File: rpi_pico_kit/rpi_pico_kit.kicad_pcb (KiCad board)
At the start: 2 copper layers, 99.1 x 99.1 mm, 200 parts, among them J1 DC Jack 5.5x2.1mm, J10 OLED Display SSD1306, J11 Conn_01x04_Male, J12 Conn_01x04_Male, J13 AudioJack-CUI-SJ-3523-SMT, J14 AudioJack-CUI-SJ-3523-SMT, J2 USB_B, J3 Conn_01x03_Male, J4 DB15_Female, J5 HDMI_A, J6 Conn_01x08_Male, J7 Conn_01x08_Male, J8 Conn_01x08_Male, J9 Micro_SD_Card_Det, Q1 DMN63D8L-7, Q2 DMN63D8L-7, Q3 DMN63D8L-7, Q4 DMN63D8L-7, Q5 DMN63D8L-7, Q6 DMN63D8L-7, Q7 DMN63D8L-7, SW1 SW_Push, SW10 SW_Push, SW2 RotaryEncoder_Switch, SW3 SW_Push, SW4 SW_Push, SW5 SW_Push, SW6 SW_Push, SW7 SW_Push, SW8 SW_Push, SW9 SW_Push, U1 RPi Pico, U10 74LVC2G34GV, U11 PCM5101A, U2 NCP1117-3.3_SOT223, U3 RP2040, U4 W25Q16JVSSIQ, U5 74HC14, U6 74HC14, U7 MCP23S08-xSO, U8 AT24CS32, U9 NCP115-3.3_SOT23-5, Y1 12MHz

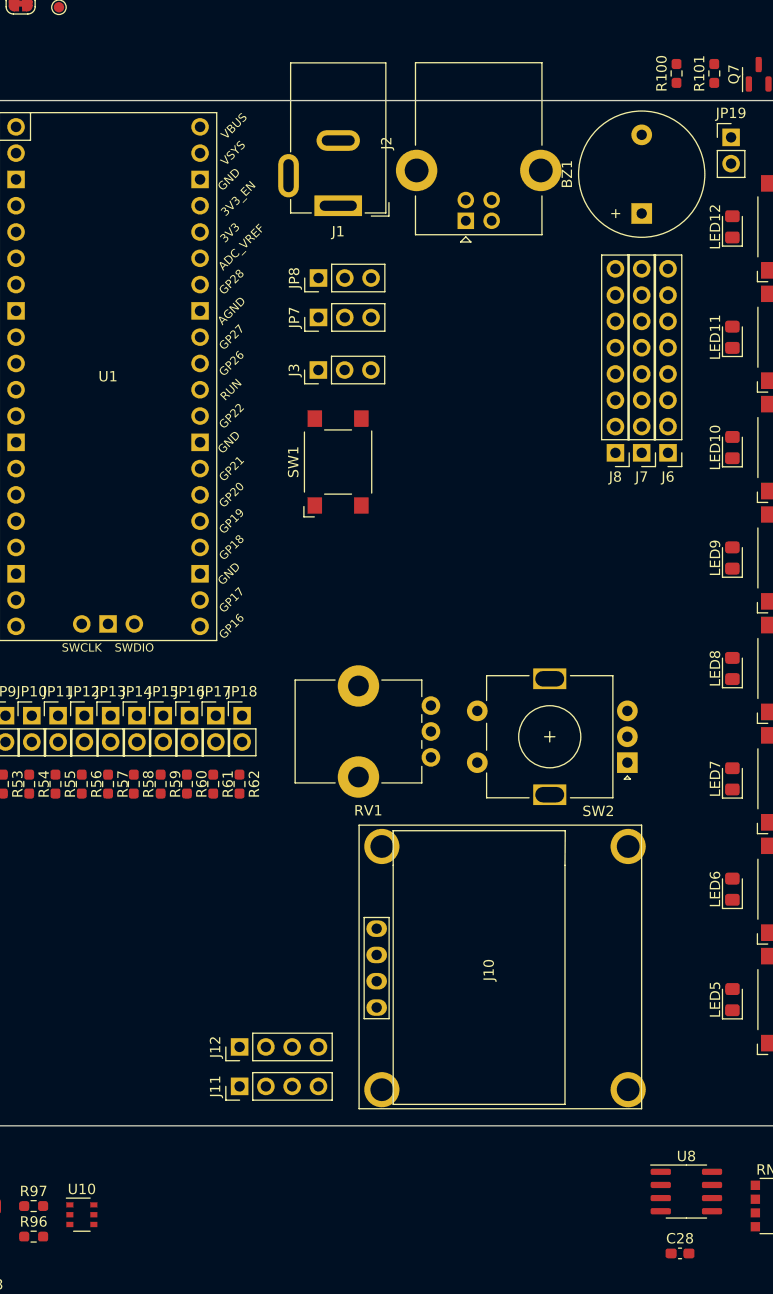
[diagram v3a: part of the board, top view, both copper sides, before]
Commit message: changed footprint U10
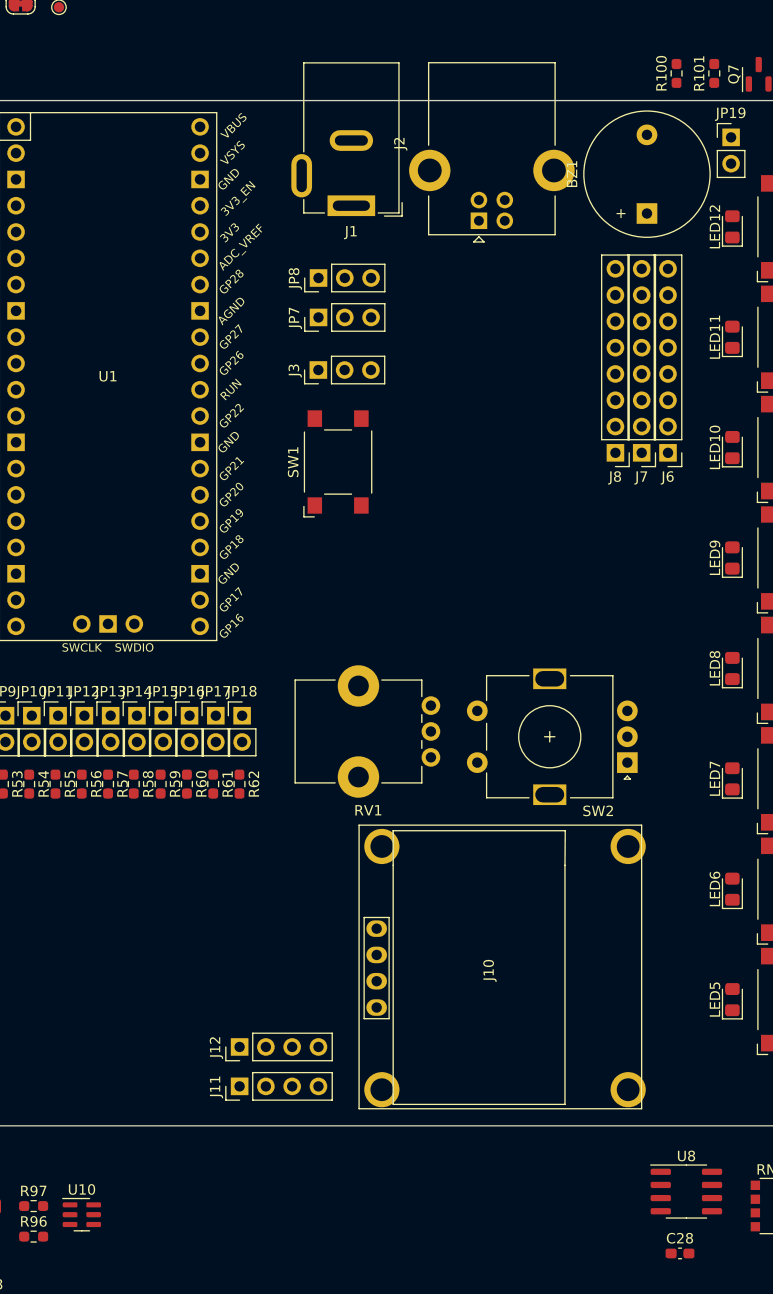
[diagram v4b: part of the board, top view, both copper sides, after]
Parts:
- U10: footprint Package_SO:TSOP-6_1.65x3.05mm_P0.95mm -> Package_SO:SC-74-6_1.5x2.9mm_P0.95mm
- moved J2 1.27 mm to (103.1, 49.7)
- moved J1 1.27 mm to (90.8, 48.3)
- moved BZ1 0.51 mm to (119.4, 49.0)
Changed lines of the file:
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@@
     )
   )
-  (footprint "Package_SO:TSOP-6_1.65x3.05mm_P0.95mm" (layer "F.Cu")
+  (footprint "Package_SO:SC-74-6_1.5x2.9mm_P0.95mm" (layer "F.Cu")
     (at 64.78 145.745)
-    (descr "TSOP-6 package (comparable to TSOT-23), https://www.vishay.com/docs/71200/71200.pdf")
-    (tags "Jedec MO-193C TSOP-6L")
+    (descr "SC-74, 6 Pin (https://www.nxp.com/docs/en/package-information/SOT457.pdf), generated with kicad-footprint-generator ipc_gullwing_generator.py")
+    (tags "SC-74 SO")
     (property "Manufacturer Part Number" "74LVC2G34GV,125")
     (property "Sheetfile" "audio.kicad_sch")
@@
     (property "Supplier Part URL" "https://www.digikey.cz/en/products/detail/nexperia-usa-inc/74LVC2G34GV-125/1231596")
     (attr smd)
-    (fp_text reference "U10" (at 0 -2.45) (layer "F.SilkS")
+    (fp_text reference "U10" (at 0 -2.4) (layer "F.SilkS")
         (effects (font (size 1 1) (thickness 0.15)))
     )
-    (fp_text value "74LVC2G34GV" (at 0 2.5) (layer "F.Fab")
+    (fp_text value "74LVC2G34GV" (at 0 2.4) (layer "F.Fab")
         (effects (font (size 1 1) (thickness 0.15)))
     )
-    (fp_text user "${REFERENCE}" (at 0 0 90) (layer "F.Fab")
-        (effects (font (size 0.5 0.5) (thickness 0.075)))
+    (fp_text user "${REFERENCE}" (at 0 0) (layer "F.Fab")
+        (effects (font (size 0.38 0.38) (thickness 0.06)))
     )
-    (fp_line (start -0.8 1.6) (end 0.8 1.6)
+    (fp_line (start 0 -1.56) (end -1.85 -1.56)
+      (stroke (width 0.12) (type solid)) (layer "F.SilkS"))
+    (fp_line (start 0 -1.56) (end 0.75 -1.56)
+      (stroke (width 0.12) (type solid)) (layer "F.SilkS"))
+    (fp_line (start 0 1.56) (end -0.75 1.56)
       (stroke (width 0.12) (type solid)) (layer "F.SilkS"))
-    (fp_line (start 0.8 -1.6) (end -1.5 -1.6)
+    (fp_line (start 0 1.56) (end 0.75 1.56)
       (stroke (width 0.12) (type solid)) (layer "F.SilkS"))
-    (fp_line (start -1.76 -1.78) (end -1.76 1.77)
+    (fp_line (start -2.1 -1.7) (end -2.1 1.7)
       (stroke (width 0.05) (type solid)) (layer "F.CrtYd"))
-    (fp_line (start -1.76 -1.78) (end 1.76 -1.78)
+    (fp_line (start -2.1 1.7) (end 2.1 1.7)
       (stroke (width 0.05) (type solid)) (layer "F.CrtYd"))
-    (fp_line (start 1.76 1.77) (end -1.76 1.77)
+    (fp_line (start 2.1 -1.7) (end -2.1 -1.7)
       (stroke (width 0.05) (type solid)) (layer "F.CrtYd"))
-    (fp_line (start 1.76 1.77) (end 1.76 -1.78)
+    (fp_line (start 2.1 1.7) (end 2.1 -1.7)
       (stroke (width 0.05) (type solid)) (layer "F.CrtYd"))
-    (fp_line (start -0.825 -1.1) (end -0.825 1.525)
+    (fp_line (start -0.75 -1.075) (end -0.375 -1.45)
       (stroke (width 0.1) (type solid)) (layer "F.Fab"))
-    (fp_line (start -0.825 -1.1) (end -0.425 -1.525)
+    (fp_line (start -0.75 1.45) (end -0.75 -1.075)
       (stroke (width 0.1) (type solid)) (layer "F.Fab"))
-    (fp_line (start 0.825 -1.525) (end -0.425 -1.525)
+    (fp_line (start -0.375 -1.45) (end 0.75 -1.45)
       (stroke (width 0.1) (type solid)) (layer "F.Fab"))
-    (fp_line (start 0.825 -1.525) (end 0.825 1.525)
+    (fp_line (start 0.75 -1.45) (end 0.75 1.45)
       (stroke (width 0.1) (type solid)) (layer "F.Fab"))
-    (fp_line (start 0.825 1.525) (end -0.825 1.525)
+    (fp_line (start 0.75 1.45) (end -0.75 1.45)
       (stroke (width 0.1) (type solid)) (layer "F.Fab"))
-    (pad "1" smd rect (at -1.16 -0.95) (size 0.7 0.51) (layers "F.Cu" "F.Paste" "F.Mask")
+    (pad "1" smd roundrect (at -1.1375 -0.95) (size 1.425 0.5) (layers "F.Cu" "F.Paste" "F.Mask") (roundrect_rratio 0.25)
       (net 136 "/I2S_LRCK") (pinfunction "A1") (pintype "input"))
-    (pad "2" smd rect (at -1.16 0) (size 0.7 0.51) (layers "F.Cu" "F.Paste" "F.Mask")
+    (pad "2" smd roundrect (at -1.1375 0) (size 1.425 0.5) (layers "F.Cu" "F.Paste" "F.Mask") (roundrect_rratio 0.25)
       (net 3 "GND") (pinfunction "GND") (pintype "power_in"))
-    (pad "3" smd rect (at -1.16 0.95) (size 0.7 0.51) (layers "F.Cu" "F.Paste" "F.Mask")
+    (pad "3" smd roundrect (at -1.1375 0.95) (size 1.425 0.5) (layers "F.Cu" "F.Paste" "F.Mask") (roundrect_rratio 0.25)
       (net 137 "/I2S_BCK") (pinfunction "A2") (pintype "input"))
-    (pad "4" smd rect (at 1.16 0.95) (size 0.7 0.51) (layers "F.Cu" "F.Paste" "F.Mask")
+    (pad "4" smd roundrect (at 1.1375 0.95) (size 1.425 0.5) (layers "F.Cu" "F.Paste" "F.Mask") (roundrect_rratio 0.25)
       (net 151 "Net-(U10-Y2)") (pinfunction "Y2") (pintype "output"))
-    (pad "5" smd rect (at 1.16 0) (size 0.7 0.51) (layers "F.Cu" "F.Paste" "F.Mask")
+    (pad "5" smd roundrect (at 1.1375 0) (size 1.425 0.5) (layers "F.Cu" "F.Paste" "F.Mask") (roundrect_rratio 0.25)
       (net 12 "+3.3VA") (pinfunction "VCC") (pintype "power_in"))
-    (pad "6" smd rect (at 1.16 -0.95) (size 0.7 0.51) (layers "F.Cu" "F.Paste" "F.Mask")
+    (pad "6" smd roundrect (at 1.1375 -0.95) (size 1.425 0.5) (layers "F.Cu" "F.Paste" "F.Mask") (roundrect_rratio 0.25)
       (net 150 "Net-(U10-Y1)") (pinfunction "Y1") (pintype "output"))
     (model "${KICAD6_3DMODEL_DIR}/Package_SO.3dshapes/TSOP-6_1.65x3.05mm_P0.95mm.wrl"
@@
   )
   (footprint "Connector_BarrelJack:BarrelJack_GCT_DCJ200-10-A_Horizontal" (layer "F.Cu")
-    (at 89.55 48.26 180)
+    (at 90.82 48.26 180)
     (descr "Barrel jack connector (5.5 mm outer diameter, 2.05 inner diameter ), https://gct.co/files/drawings/dcj200-10.pdf")
     (tags "connector barrel jack")
@@
   )
   (footprint "Buzzer_Beeper:Buzzer_12x9.5RM7.6" (layer "F.Cu")
-    (at 118.872 49.012 90)
+    (at 119.38 49.012 90)
     (descr "Generic Buzzer, D12mm height 9.5mm with RM7.6mm")
     (tags "buzzer")
@@
   )
   (footprint "Connector_USB:USB_B_Lumberg_2411_02_Horizontal" (layer "F.Cu")
-    (at 101.874 49.7135 90)
+    (at 103.144 49.7135 90)
     (descr "USB 2.0 receptacle type B, horizontal version, through-hole, https://downloads.lumberg.com/datenblaetter/en/2411_02.pdf")
     (tags "USB B receptacle horizontal through-hole")

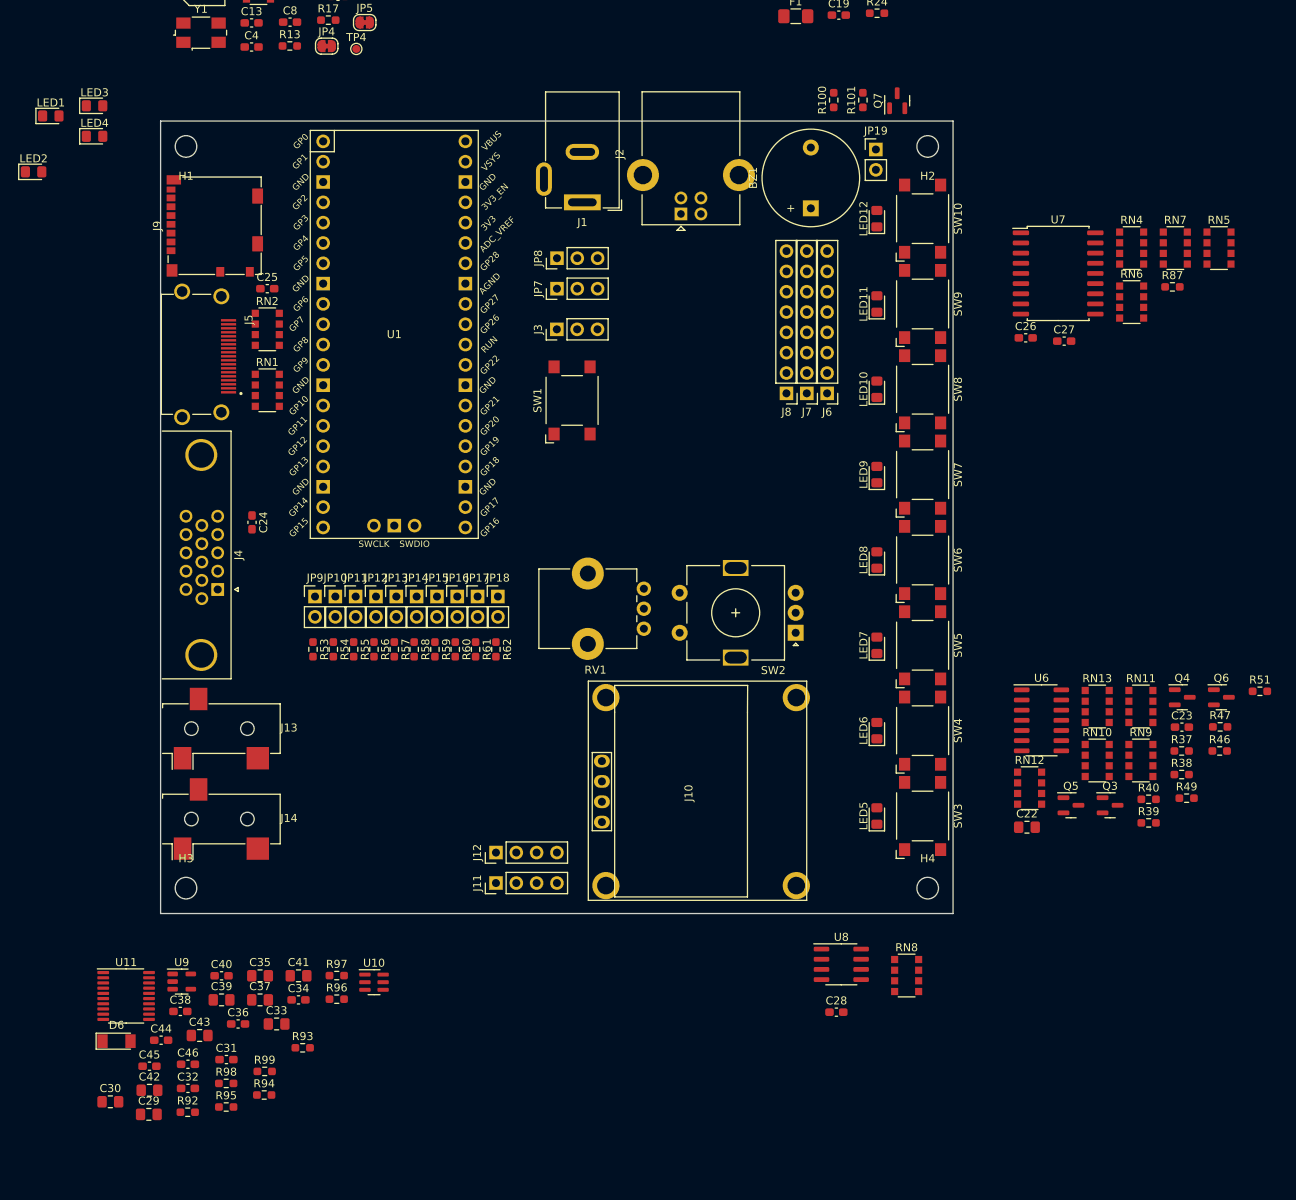
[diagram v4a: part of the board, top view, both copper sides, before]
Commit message: SPI conflict solved
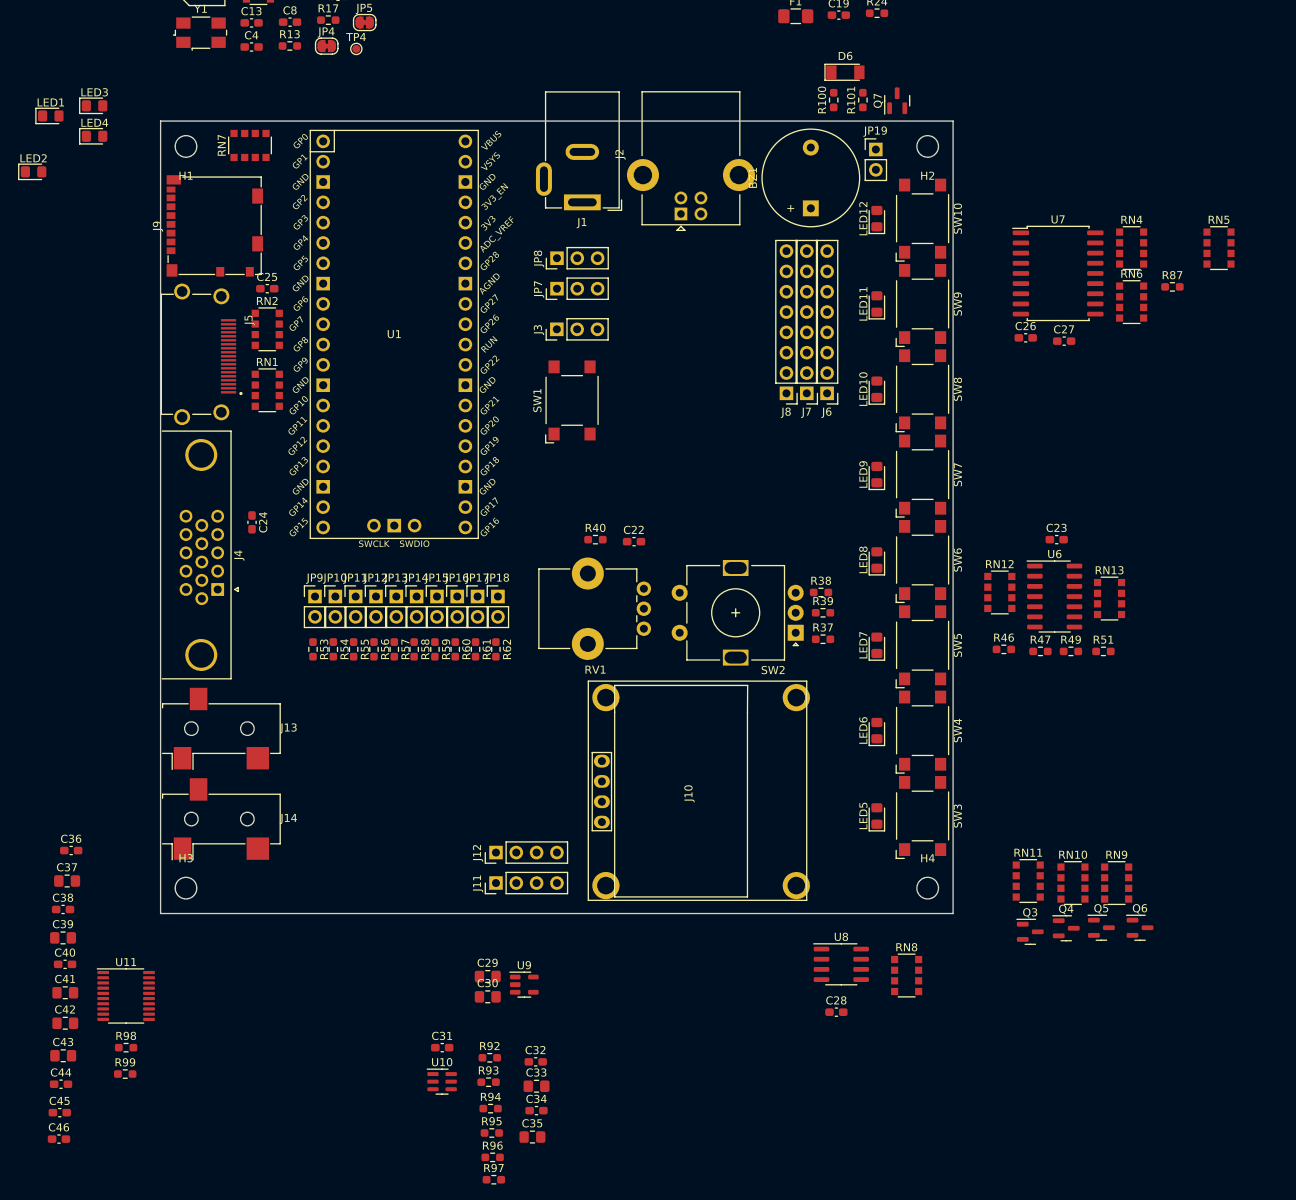
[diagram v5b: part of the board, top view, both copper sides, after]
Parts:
- C22: footprint Capacitor_SMD:C_0805_2012Metric_Pad1.18x1.45mm_HandSolder -> Capacitor_SMD:C_0603_1608Metric_Pad1.08x0.95mm_HandSolder
- moved D6 151.6 mm to (123.7, 32.0)
- moved RN7 116.4 mm to (49.3, 41.1), turned to 90 degrees
- moved R40 76.4 mm to (92.5, 90.4)
- moved C22 60.7 mm to (97.3, 90.7)
- moved R38 50.5 mm to (120.7, 97.0)
- moved C30 49.0 mm to (79.0, 147.6)
- moved R39 48.4 mm to (120.9, 99.6)
- moved R37 47.0 mm to (120.9, 102.9)
- moved C29 45.7 mm to (79.0, 145.0)
- moved C32 43.6 mm to (85.0, 155.7)
- moved U9 42.8 mm to (83.6, 146.1)
- moved C35 39.6 mm to (84.6, 165.1)
- moved R92 38.4 mm to (79.2, 155.2)
- moved C33 33.4 mm to (85.1, 158.8)
- moved R95 33.4 mm to (79.5, 164.6)
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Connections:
- J9 pad 2: /SD_CS -> /SPI Devices/SD_CS
- J9 pad 3: /LED2 -> /SPI Devices/MOSI
- J9 pad 5: /LED1 -> /SPI Devices/SCK
- J9 pad 7: /SPI_MISO -> /SPI Devices/MISO
- R87 pad 1: /SD_CS -> /SPI_EXPANDER_CS
- R87 pad 2: /SD_CS -> /SPI Devices/EXPANDER_CS
- RN7 pad 4: /EXPANDER_CS -> /SPI_SD_CS
- RN7 pad 5: /EXPANDER_CS -> /SPI Devices/SD_CS
- RN7 pad 6: /LED2 -> /SPI Devices/MOSI
- RN7 pad 7: /SPI_MISO -> /SPI Devices/MISO
- RN7 pad 8: /LED1 -> /SPI Devices/SCK
- U1 pad 31: /EXPANDER_CS -> /SPI_EXPANDER_CS
- U1 pad 7: /SD_CS -> /SPI_SD_CS
- U7 pad 1: /LED1 -> /SPI Devices/SCK
- U7 pad 2: /LED2 -> /SPI Devices/MOSI
- U7 pad 3: /SPI_MISO -> /SPI Devices/MISO
- U7 pad 7: /EXPANDER_CS -> /SPI Devices/EXPANDER_CS

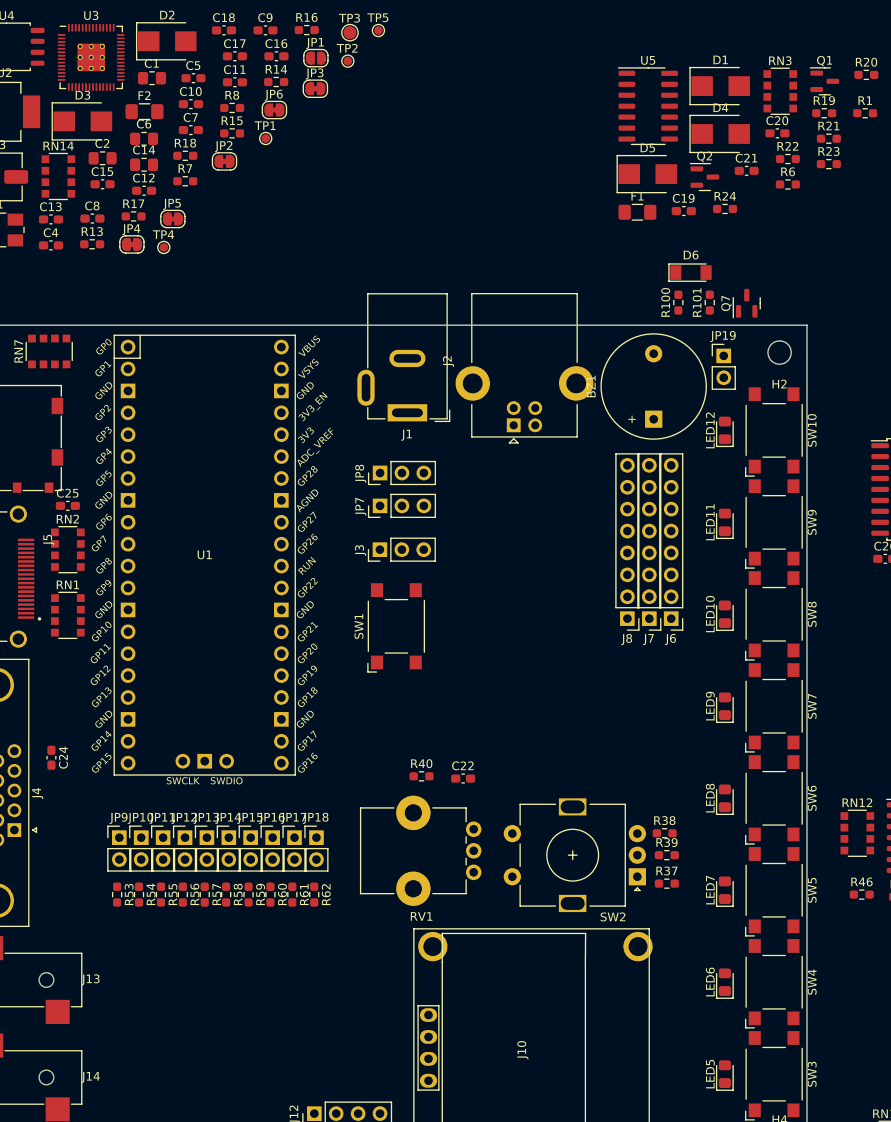
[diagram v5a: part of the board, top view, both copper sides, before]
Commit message: changed footprint for diodes
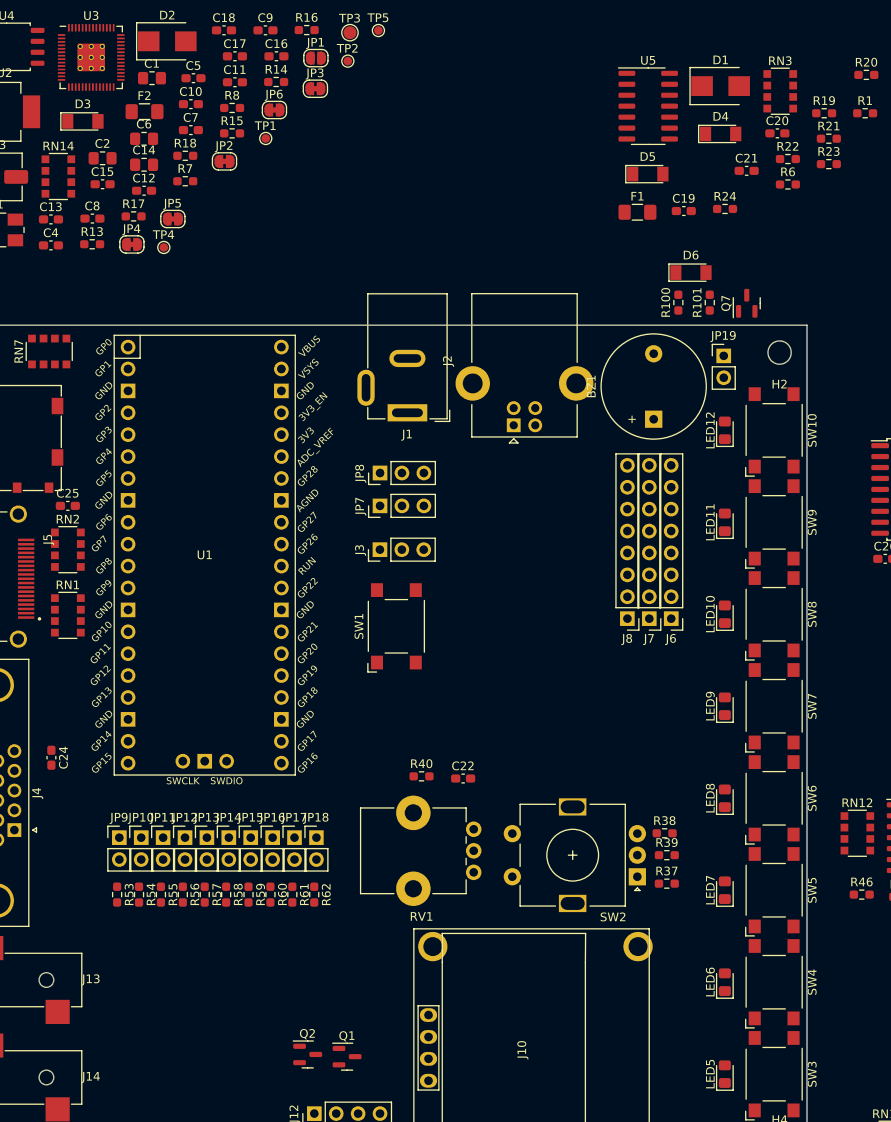
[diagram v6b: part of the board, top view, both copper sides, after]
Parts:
- D3, D4, D5: value STPS1L30U -> LL101B-GS18; footprint Diode_SMD:D_SMB -> Diode_SMD:D_MiniMELF
- moved Q1 126.0 mm to (83.8, 122.9)
- moved Q2 111.7 mm to (79.2, 122.7)
